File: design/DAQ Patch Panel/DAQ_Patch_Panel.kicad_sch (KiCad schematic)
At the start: 4 parts, among them J1 Power Terminal 1, J2 Data Output Terminal, J3 Power Terminal 2, J4 12-Pole-PCB-Triple-Layer-Conn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

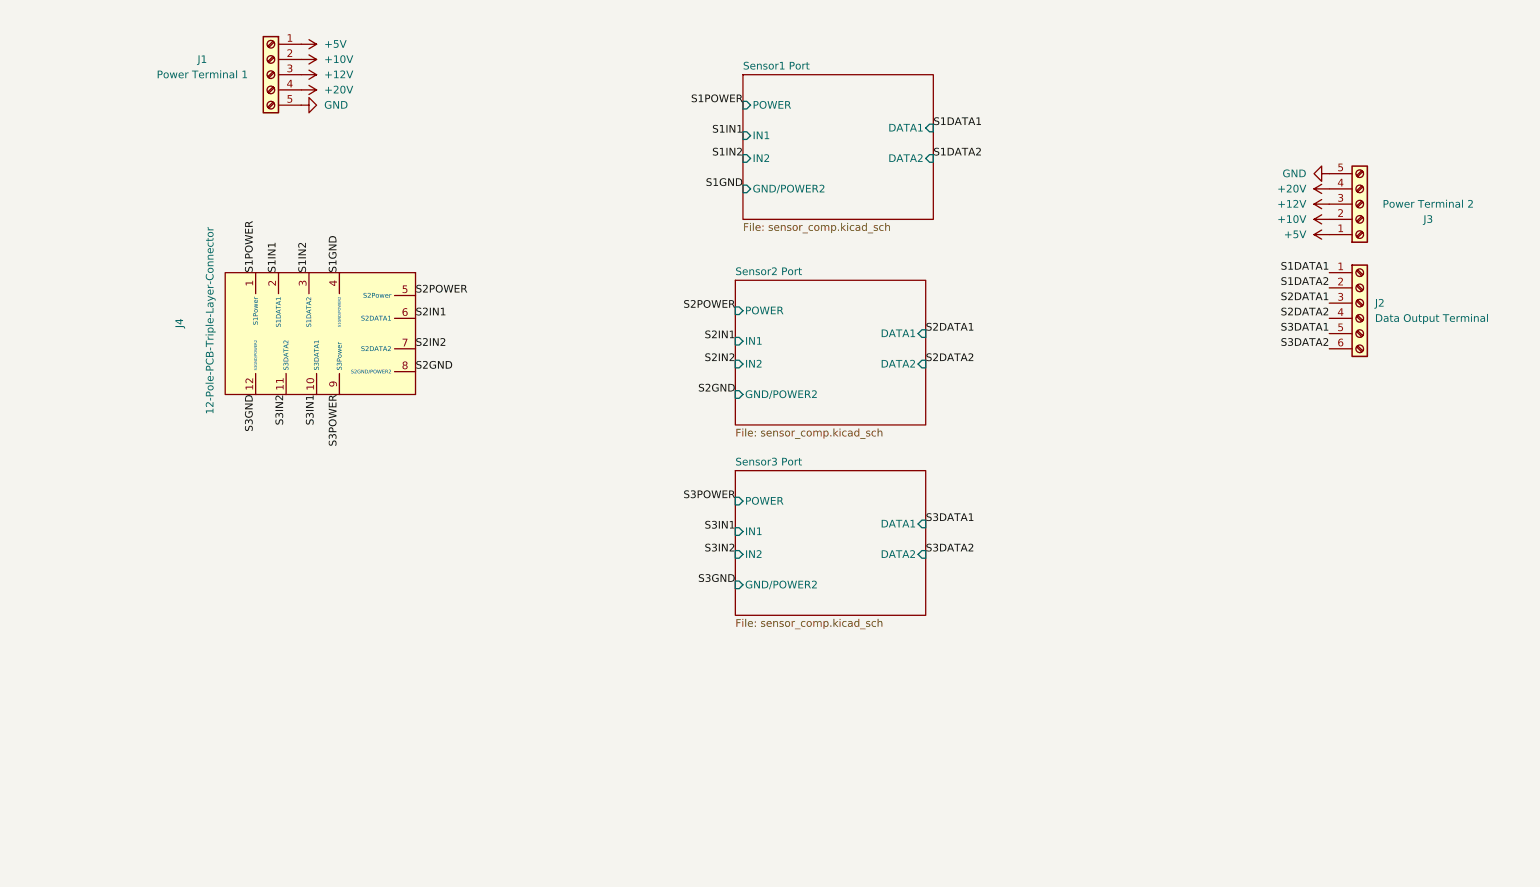
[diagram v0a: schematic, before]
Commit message: Files Renamed and Changes Implemented
Renamed project to Daq Patch Panel
Updated 4 way jumper footprints
Renamed input screw terminal
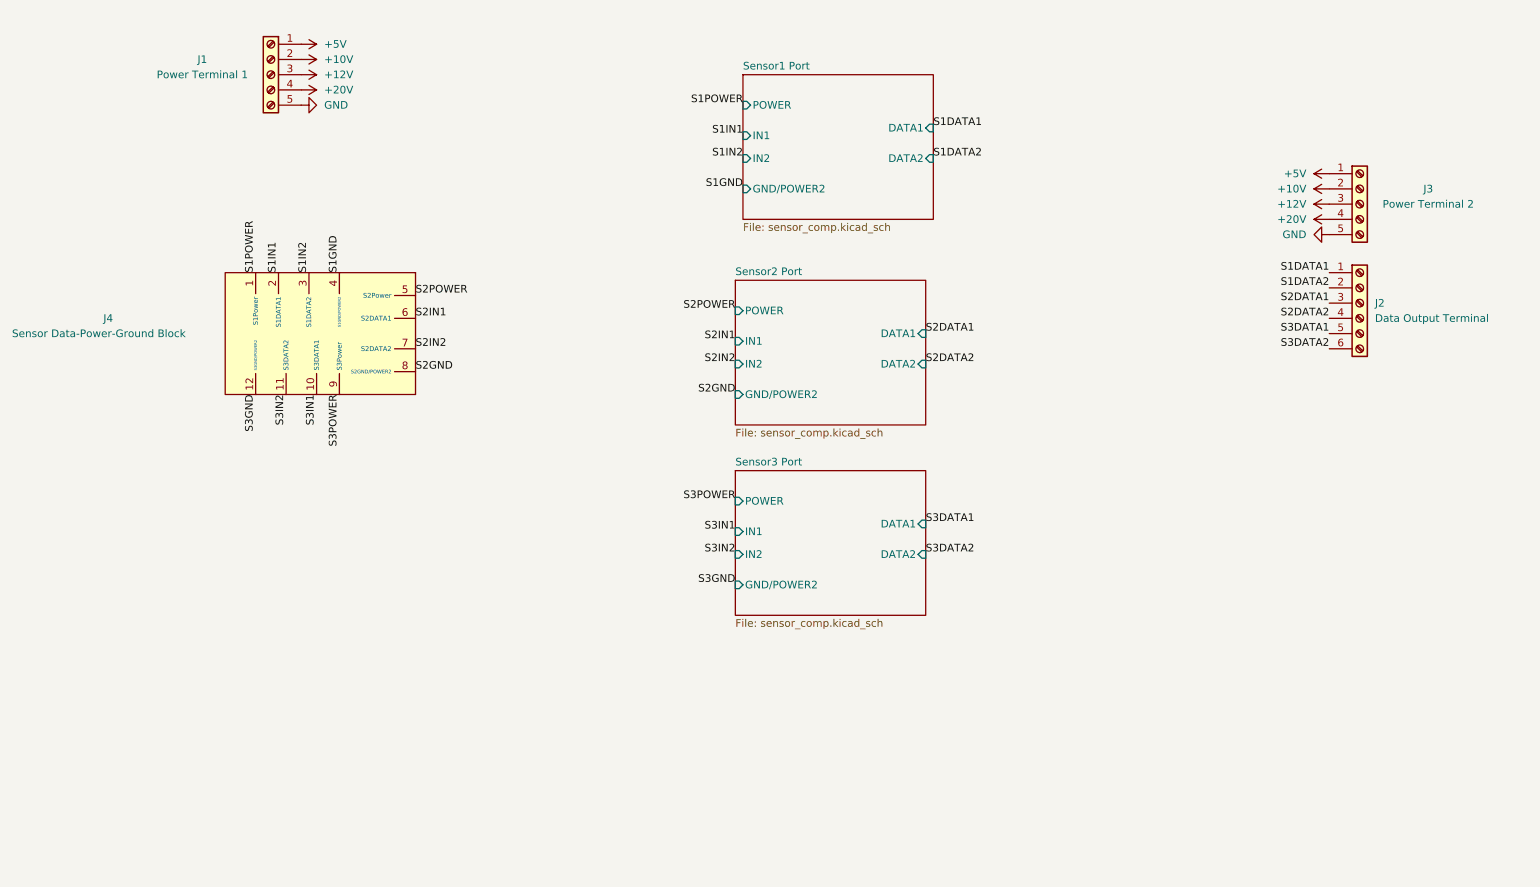
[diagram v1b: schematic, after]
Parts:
- J4: value 12-Pole-PCB-Triple-Layer-Connector -> Sensor Data-Power-Ground Block
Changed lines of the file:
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@@
     (pin "6")
     (instances
-      (project "DAQ_Power_Patch"
+      (project "DAQ_Patch_Panel"
         (path "/da75d2ac-4c40-407d-8f74-3497a5ffc88d"
           (reference "J2") (unit 1)
@@
     (pin "1")
     (instances
-      (project "DAQ_Power_Patch"
+      (project "DAQ_Patch_Panel"
         (path "/da75d2ac-4c40-407d-8f74-3497a5ffc88d"
           (reference "#PWR014") (unit 1)
@@
     )
   )
-  (symbol (lib_name "+10V_1") (lib_id "power:+10V") (at 238.76 69.85 90) (mirror x) (unit 1)
-    (in_bom yes) (on_board yes) (dnp no) (fields_autoplaced)
-    (property "Reference" "#PWR020" (at 242.57 69.85 0)
-      (effects (font (size 1.27 1.27)) hide)
-    )
-    (property "Value" "+20V" (at 234.95 69.85 90)
-      (effects (font (size 1.27 1.27)) (justify left))
-    )
-    (property "Footprint" "" (at 238.76 69.85 0)
-      (effects (font (size 1.27 1.27)) hide)
-    )
-    (property "Datasheet" "" (at 238.76 69.85 0)
-      (effects (font (size 1.27 1.27)) hide)
-    )
-    (pin "1")
-    (instances
-      (project "DAQ_Power_Patch"
+  (symbol (lib_name "+10V_1") (lib_id "power:+10V") (at 238.76 74.93 90) (mirror x) (unit 1)
+    (in_bom yes) (on_board yes) (dnp no)
+    (property "Reference" "#PWR020" (at 242.57 74.93 0)
+      (effects (font (size 1.27 1.27)) hide)
+    )
+    (property "Value" "+20V" (at 234.95 74.93 90)
+      (effects (font (size 1.27 1.27)) (justify left))
+    )
+    (property "Footprint" "" (at 238.76 74.93 0)
+      (effects (font (size 1.27 1.27)) hide)
+    )
+    (property "Datasheet" "" (at 238.76 74.93 0)
+      (effects (font (size 1.27 1.27)) hide)
+    )
+    (pin "1")
+    (instances
+      (project "DAQ_Patch_Panel"
         (path "/da75d2ac-4c40-407d-8f74-3497a5ffc88d"
           (reference "#PWR020") (unit 1)
@@
     (pin "1")
     (instances
-      (project "DAQ_Power_Patch"
+      (project "DAQ_Patch_Panel"
         (path "/da75d2ac-4c40-407d-8f74-3497a5ffc88d"
           (reference "#PWR013") (unit 1)
@@
     )
   )
-  (symbol (lib_id "power:+5V") (at 238.76 77.47 90) (mirror x) (unit 1)
-    (in_bom yes) (on_board yes) (dnp no) (fields_autoplaced)
-    (property "Reference" "#PWR015" (at 242.57 77.47 0)
-      (effects (font (size 1.27 1.27)) hide)
-    )
-    (property "Value" "+5V" (at 234.95 77.47 90)
-      (effects (font (size 1.27 1.27)) (justify left))
-    )
-    (property "Footprint" "" (at 238.76 77.47 0)
-      (effects (font (size 1.27 1.27)) hide)
-    )
-    (property "Datasheet" "" (at 238.76 77.47 0)
-      (effects (font (size 1.27 1.27)) hide)
-    )
-    (pin "1")
-    (instances
-      (project "DAQ_Power_Patch"
+  (symbol (lib_id "power:+5V") (at 238.76 67.31 90) (mirror x) (unit 1)
+    (in_bom yes) (on_board yes) (dnp no)
+    (property "Reference" "#PWR015" (at 242.57 67.31 0)
+      (effects (font (size 1.27 1.27)) hide)
+    )
+    (property "Value" "+5V" (at 234.95 67.31 90)
+      (effects (font (size 1.27 1.27)) (justify left))
+    )
+    (property "Footprint" "" (at 238.76 67.31 0)
+      (effects (font (size 1.27 1.27)) hide)
+    )
+    (property "Datasheet" "" (at 238.76 67.31 0)
+      (effects (font (size 1.27 1.27)) hide)
+    )
+    (pin "1")
+    (instances
+      (project "DAQ_Patch_Panel"
         (path "/da75d2ac-4c40-407d-8f74-3497a5ffc88d"
           (reference "#PWR015") (unit 1)
@@
   )
   (symbol (lib_id "power:+12V") (at 238.76 72.39 90) (mirror x) (unit 1)
-    (in_bom yes) (on_board yes) (dnp no) (fields_autoplaced)
+    (in_bom yes) (on_board yes) (dnp no)
     (property "Reference" "#PWR019" (at 242.57 72.39 0)
       (effects (font (size 1.27 1.27)) hide)
@@
     (pin "1")
     (instances
-      (project "DAQ_Power_Patch"
+      (project "DAQ_Patch_Panel"
         (path "/da75d2ac-4c40-407d-8f74-3497a5ffc88d"
           (reference "#PWR019") (unit 1)
@@
     (pin "5")
     (instances
-      (project "DAQ_Power_Patch"
+      (project "DAQ_Patch_Panel"
         (path "/da75d2ac-4c40-407d-8f74-3497a5ffc88d"
           (reference "J1") (unit 1)
@@
     (pin "1")
     (instances
-      (project "DAQ_Power_Patch"
+      (project "DAQ_Patch_Panel"
         (path "/da75d2ac-4c40-407d-8f74-3497a5ffc88d"
           (reference "#PWR011") (unit 1)
@@
     )
   )
-  (symbol (lib_id "power:GND") (at 238.76 67.31 270) (mirror x) (unit 1)
-    (in_bom yes) (on_board yes) (dnp no) (fields_autoplaced)
-    (property "Reference" "#PWR021" (at 232.41 67.31 0)
-      (effects (font (size 1.27 1.27)) hide)
-    )
-    (property "Value" "GND" (at 234.95 67.31 90)
-      (effects (font (size 1.27 1.27)) (justify right))
-    )
-    (property "Footprint" "" (at 238.76 67.31 0)
-      (effects (font (size 1.27 1.27)) hide)
-    )
-    (property "Datasheet" "" (at 238.76 67.31 0)
-      (effects (font (size 1.27 1.27)) hide)
-    )
-    (pin "1")
-    (instances
-      (project "DAQ_Power_Patch"
+  (symbol (lib_id "power:GND") (at 238.76 77.47 270) (mirror x) (unit 1)
+    (in_bom yes) (on_board yes) (dnp no)
+    (property "Reference" "#PWR021" (at 232.41 77.47 0)
+      (effects (font (size 1.27 1.27)) hide)
+    )
+    (property "Value" "GND" (at 234.95 77.47 90)
+      (effects (font (size 1.27 1.27)) (justify right))
+    )
+    (property "Footprint" "" (at 238.76 77.47 0)
+      (effects (font (size 1.27 1.27)) hide)
+    )
+    (property "Datasheet" "" (at 238.76 77.47 0)
+      (effects (font (size 1.27 1.27)) hide)
+    )
+    (pin "1")
+    (instances
+      (project "DAQ_Patch_Panel"
         (path "/da75d2ac-4c40-407d-8f74-3497a5ffc88d"
           (reference "#PWR021") (unit 1)
@@
     (pin "1")
     (instances
-      (project "DAQ_Power_Patch"
+      (project "DAQ_Patch_Panel"
         (path "/da75d2ac-4c40-407d-8f74-3497a5ffc88d"
           (reference "#PWR012") (unit 1)
@@
     )
   )
-  (symbol (lib_id "Connector:Screw_Terminal_01x05") (at 243.84 72.39 0) (mirror x) (unit 1)
-    (in_bom yes) (on_board yes) (dnp no)
-    (property "Reference" "J3" (at 255.27 74.93 0)
+  (symbol (lib_id "Connector:Screw_Terminal_01x05") (at 243.84 72.39 0) (unit 1)
+    (in_bom yes) (on_board yes) (dnp no)
+    (property "Reference" "J3" (at 255.27 69.85 0)
       (effects (font (size 1.27 1.27)))
     )
@@
     (pin "5")
     (instances
-      (project "DAQ_Power_Patch"
+      (project "DAQ_Patch_Panel"
         (path "/da75d2ac-4c40-407d-8f74-3497a5ffc88d"
           (reference "J3") (unit 1)
@@
     (pin "1")
     (instances
-      (project "DAQ_Power_Patch"
+      (project "DAQ_Patch_Panel"
         (path "/da75d2ac-4c40-407d-8f74-3497a5ffc88d"
           (reference "#PWR010") (unit 1)
@@
   (symbol (lib_id "DAQLibrary:12-Pole-PCB-Triple-Layer-Connector") (at 72.39 92.71 270) (unit 1)
     (in_bom yes) (on_board yes) (dnp no)
-    (property "Reference" "J4" (at 46.99 91.44 0)
-      (effects (font (size 1.27 1.27)) (justify left))
-    )
-    (property "Value" "12-Pole-PCB-Triple-Layer-Connector" (at 52.07 76.2 0)
+    (property "Reference" "J4" (at 34.29 91.44 90)
+      (effects (font (size 1.27 1.27)) (justify left))
+    )
+    (property "Value" "Sensor Data-Power-Ground Block" (at 19.05 93.98 90)
       (effects (font (size 1.27 1.27)) (justify left))
     )
@@
     (pin "9")
     (instances
-      (project "DAQ_Power_Patch"
+      (project "DAQ_Patch_Panel"
         (path "/da75d2ac-4c40-407d-8f74-3497a5ffc88d"
           (reference "J4") (unit 1)
@@
     )
   )
-  (symbol (lib_id "power:+10V") (at 238.76 74.93 90) (mirror x) (unit 1)
-    (in_bom yes) (on_board yes) (dnp no) (fields_autoplaced)
-    (property "Reference" "#PWR017" (at 242.57 74.93 0)
-      (effects (font (size 1.27 1.27)) hide)
-    )
-    (property "Value" "+10V" (at 234.95 74.93 90)
-      (effects (font (size 1.27 1.27)) (justify left))
-    )
-    (property "Footprint" "" (at 238.76 74.93 0)
-      (effects (font (size 1.27 1.27)) hide)
-    )
-    (property "Datasheet" "" (at 238.76 74.93 0)
-      (effects (font (size 1.27 1.27)) hide)
-    )
-    (pin "1")
-    (instances
-      (project "DAQ_Power_Patch"
+  (symbol (lib_id "power:+10V") (at 238.76 69.85 90) (mirror x) (unit 1)
+    (in_bom yes) (on_board yes) (dnp no)
+    (property "Reference" "#PWR017" (at 242.57 69.85 0)
+      (effects (font (size 1.27 1.27)) hide)
+    )
+    (property "Value" "+10V" (at 234.95 69.85 90)
+      (effects (font (size 1.27 1.27)) (justify left))
+    )
+    (property "Footprint" "" (at 238.76 69.85 0)
+      (effects (font (size 1.27 1.27)) hide)
+    )
+    (property "Datasheet" "" (at 238.76 69.85 0)
+      (effects (font (size 1.27 1.27)) hide)
+    )
+    (pin "1")
+    (instances
+      (project "DAQ_Patch_Panel"
         (path "/da75d2ac-4c40-407d-8f74-3497a5ffc88d"
           (reference "#PWR017") (unit 1)
@@
     )
     (instances
-      (project "DAQ_Power_Patch"
+      (project "DAQ_Patch_Panel"
         (path "/da75d2ac-4c40-407d-8f74-3497a5ffc88d" (page "3"))
       )
@@
     )
     (instances
-      (project "DAQ_Power_Patch"
+      (project "DAQ_Patch_Panel"
         (path "/da75d2ac-4c40-407d-8f74-3497a5ffc88d" (page "2"))
       )
@@
     )
     (instances
-      (project "DAQ_Power_Patch"
+      (project "DAQ_Patch_Panel"
         (path "/da75d2ac-4c40-407d-8f74-3497a5ffc88d" (page "4"))
       )

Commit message: Latest Review Changes
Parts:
- removed J4: Sensor Data-Power-Ground Block, Library:Weidmuller LM3RZF, symbol DAQLibrary:12-Pole-PCB-Triple-Layer-Connector
- added J4: Weidmuller LM3RZF, symbol DAQLibrary:Weidmuller LM3RZF
- J2: footprint Library:TerminalBlock_Phoenix_MKDS_1,5-6-5-5.08_1x06P5.08 -> TerminalBlock_Phoenix:TerminalBlock_Phoenix_MKDS-1,5-6-5.08_1x06_P5.08mm_Horizontal
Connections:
- net +10V: now also J1.3 (Pin_3), J3.3 (Pin_3); no longer J1.2 (Pin_2), J3.2 (Pin_2)
- net +12V: now also J1.2 (Pin_2), J3.2 (Pin_2); no longer J1.3 (Pin_3), J3.3 (Pin_3)
- net +20V: now also J1.1 (Pin_1), J3.1 (Pin_1); no longer J1.4 (Pin_4), J3.4 (Pin_4)
- net +5V: now also J1.4 (Pin_4), J3.4 (Pin_4); no longer J1.1 (Pin_1), J3.1 (Pin_1)
- net S1GND: now also J4.4
- net S1IN1: now also J4.2
- net S1IN2: now also J4.3
- net S1POWER: now also J4.1
- net S2GND: now also J4.4
- net S2IN1: now also J4.2
- net S2IN2: now also J4.3
- net S2POWER: now also J4.1
- net S3GND: now also J4.4
- net S3IN1: now also J4.2
- net S3IN2: now also J4.3
- net S3POWER: now also J4.1
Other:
- moved on the sheet: J1, J3

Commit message: Jack's Nitpicks Fixing
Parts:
- J4: footprint (none) -> Library:Weidmuller LM3RZF
